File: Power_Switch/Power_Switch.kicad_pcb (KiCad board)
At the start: 2 copper layers, 15 x 14 mm, 13 parts, among them J1 CONN_01X04_MALE, Q1 CSD16570Q5B, Q2 Q_NMOS_GSD, U1 MIC5060, U2 FAN4010

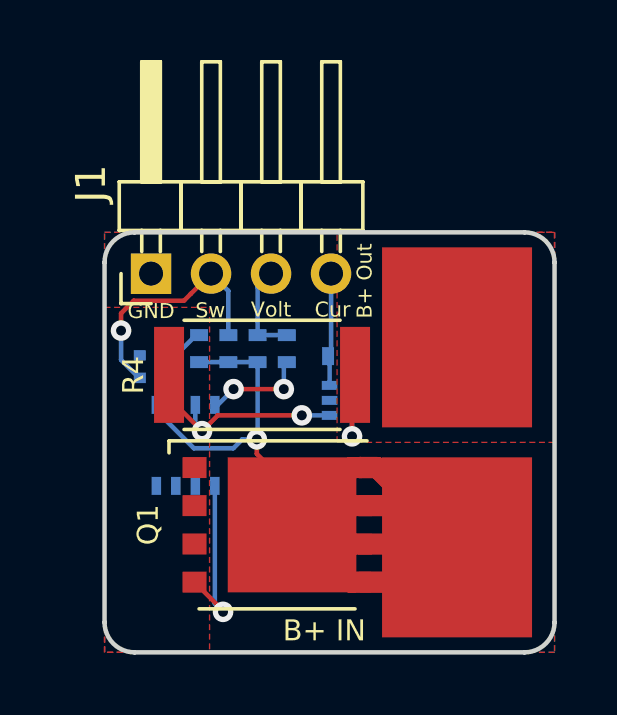
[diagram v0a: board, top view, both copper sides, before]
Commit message: Updates GPS Diamond to 1.1.
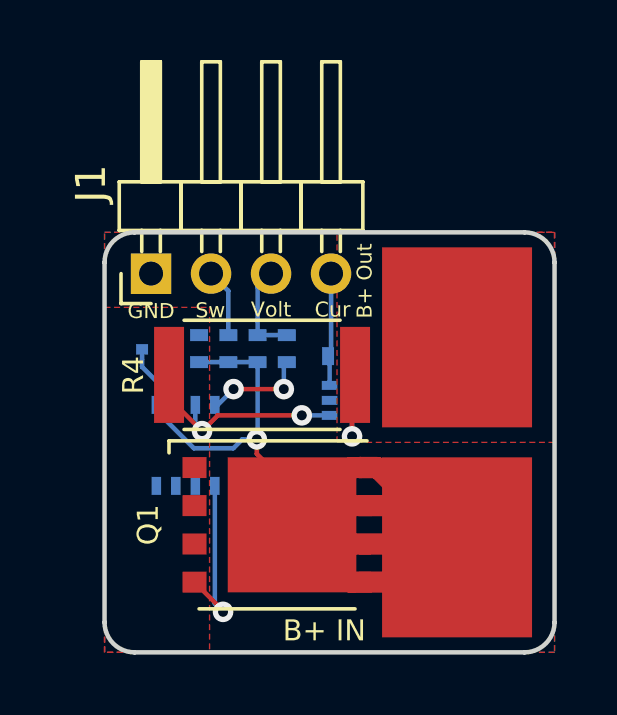
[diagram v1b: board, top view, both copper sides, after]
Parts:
- moved Q2 0.58 mm to (144.2, 96.9), turned to 270 degrees
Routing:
- net SWITCH: track 8.26 -> 2.29 mm, vias 1 -> 0
- net Net-(Q2-Pad3): track 2.95 -> 2.42 mm
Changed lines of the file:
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@@
     (links 34)
     (no_connects 0)
-    (area 142.424999 92.924999 157.575001 107.075001)
+    (area 141.1226 84.151171 157.575001 108.5274)
     (thickness 1.6002)
     (drawings 17)
-    (tracks 77)
+    (tracks 69)
     (zones 0)
     (modules 13)
@@
   )
   (module local:SOT1215 (layer B.Cu)
-    (at 144.125 97.475 90)
-    (fp_text reference Q2 (at -1.25 0 360) (layer B.SilkS)
+    (at 144.2 96.9 270)
+    (fp_text reference Q2 (at -1.25 0 540) (layer B.SilkS)
       (effects (font (size 0.5 0.5) (thickness 0.1)) (justify mirror))
     )
-    (fp_text value Q_NMOS_GSD (at 1.25 0 360) (layer B.Fab)
+    (fp_text value Q_NMOS_GSD (at 1.25 0 540) (layer B.Fab)
       (effects (font (size 0.5 0.5) (thickness 0.1)) (justify mirror))
     )
@@
     (fp_line (start 0.65 -0.75) (end 0.65 0.75) (layer B.SilkS) (width 0.15))
     (fp_line (start 0.65 0.75) (end -0.65 0.75) (layer B.SilkS) (width 0.15))
-    (pad 1 smd rect (at -0.375 -0.45 90) (size 0.35 0.4) (layers B.Cu B.Paste B.Mask)
+    (pad 1 smd rect (at -0.375 -0.45 270) (size 0.35 0.4) (layers B.Cu B.Paste B.Mask)
       (net 2 SWITCH))
-    (pad 3 smd rect (at 0 0.45 90) (size 0.35 0.4) (layers B.Cu B.Paste B.Mask)
+    (pad 3 smd rect (at 0 0.45 270) (size 0.35 0.4) (layers B.Cu B.Paste B.Mask)
       (net 9 "Net-(Q2-Pad3)"))
-    (pad 2 smd rect (at 0.375 -0.45 90) (size 0.35 0.4) (layers B.Cu B.Paste B.Mask)
+    (pad 2 smd rect (at 0.375 -0.45 270) (size 0.35 0.4) (layers B.Cu B.Paste B.Mask)
       (net 1 GND))
   )
-  (gr_text "Power Switch\nV 1.0" (at 147.05 104.1 360) (layer B.SilkS)
+  (gr_text "Power Switch\nV 1.0" (at 147.05 104.1) (layer B.SilkS)
     (effects (font (size 0.7 0.7) (thickness 0.1)) (justify mirror))
   )
@@
   (gr_line (start 157.5 94) (end 157.5 106) (layer Edge.Cuts) (width 0.15))
   (gr_line (start 142.5 94) (end 142.5 106) (layer Edge.Cuts) (width 0.15))
+  (segment (start 144.275 94.375) (end 144.05 94.375) (width 0.1524) (layer F.Cu) (net 1))
   (segment (start 148.475 98.225) (end 148.475 97.425) (width 0.1524) (layer B.Cu) (net 1))
   (segment (start 148.475 97.425) (end 148.575 97.325) (width 0.1524) (layer B.Cu) (net 1))
@@
   (segment (start 146.275 98.75) (end 146.8 98.225) (width 0.1524) (layer B.Cu) (net 1))
   (via (at 146.8 98.225) (size 0.6858) (drill 0.3302) (layers F.Cu B.Cu) (net 1))
-  (segment (start 143.05 96.275) (end 143.05 95.7) (width 0.1524) (layer F.Cu) (net 2))
-  (segment (start 143.05 95.7) (end 143.471399 95.278601) (width 0.1524) (layer F.Cu) (net 2))
-  (segment (start 143.471399 95.278601) (end 145.146399 95.278601) (width 0.1524) (layer F.Cu) (net 2))
-  (segment (start 145.146399 95.278601) (end 145.375001 95.049999) (width 0.1524) (layer F.Cu) (net 2))
-  (segment (start 145.375001 95.049999) (end 146.05 94.375) (width 0.1524) (layer F.Cu) (net 2))
-  (segment (start 143.675 97.85) (end 143.65 97.85) (width 0.1524) (layer B.Cu) (net 2))
-  (segment (start 143.65 97.85) (end 143.05 97.25) (width 0.1524) (layer B.Cu) (net 2))
-  (segment (start 143.05 97.25) (end 143.05 96.275) (width 0.1524) (layer B.Cu) (net 2))
-  (via (at 143.05 96.275) (size 0.6858) (drill 0.3302) (layers F.Cu B.Cu) (net 2))
   (segment (start 146.625 96.425) (end 146.625 94.95) (width 0.1524) (layer B.Cu) (net 2) (status 10))
   (segment (start 146.625 94.95) (end 146.05 94.375) (width 0.1524) (layer B.Cu) (net 2) (status 20))
@@
   (segment (start 150.75 99.1) (end 150.75 99.8) (width 0.1524) (layer B.Cu) (net 8) (status 10))
   (via (at 150.75 99.8) (size 0.6858) (drill 0.3302) (layers F.Cu B.Cu) (net 8))
+  (segment (start 144.875 98.75) (end 144.875 98.61) (width 0.1524) (layer B.Cu) (net 9))
+  (segment (start 144.875 98.61) (end 143.75 97.485) (width 0.1524) (layer B.Cu) (net 9))
+  (segment (start 143.75 97.485) (end 143.75 97.2274) (width 0.1524) (layer B.Cu) (net 9))
+  (segment (start 143.75 97.2274) (end 143.75 96.9) (width 0.1524) (layer B.Cu) (net 9))
   (segment (start 145.65 96.425) (end 145.55 96.425) (width 0.1524) (layer B.Cu) (net 9))
-  (segment (start 145.55 96.425) (end 144.575 97.4) (width 0.1524) (layer B.Cu) (net 9))
-  (segment (start 144.575 97.4) (end 144.575 97.475) (width 0.1524) (layer B.Cu) (net 9))
-  (segment (start 144.875 98.75) (end 144.875 97.775) (width 0.1524) (layer B.Cu) (net 9) (status 10))
-  (segment (start 144.875 97.775) (end 144.575 97.475) (width 0.1524) (layer B.Cu) (net 9) (status 20))
   (zone (net 5) (net_name "Net-(Q1-Pad1)") (layer F.Cu) (hatch edge 0.508)
     (priority 1)
@@
   )
   (zone (net 1) (net_name GND) (layer B.Cu) (hatch edge 0.508)
-    (connect_pads yes (clearance 0.2))
+    (connect_pads (clearance 0.2))
     (min_thickness 0.2)
     (fill yes (arc_segments 16) (thermal_gap 0.3) (thermal_bridge_width 0.5))
